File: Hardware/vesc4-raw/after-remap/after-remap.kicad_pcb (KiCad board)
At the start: 4 copper layers, 41.2 x 65 mm, 127 parts, among them K1 SERVO, P1 HALL/Encoder, P101 CANBUS, P2 SWD, P3 PWR_COMM, P4 IN+, P5 IN-, P6 MOTOR1, P7 MOTOR2, P9 MOTOR3, Q1 IPT007N06NATMA1, Q2 IPT007N06NATMA1, Q3 IPT007N06NATMA1, Q4 IPT007N06NATMA1, Q5 IPT007N06NATMA1, Q6 IPT007N06NATMA1, U1 STM32F40X_LQFP64, U2 TC2117, U3 DRV8302, U401 SN65HVD232, X2 8MHz 10ppm

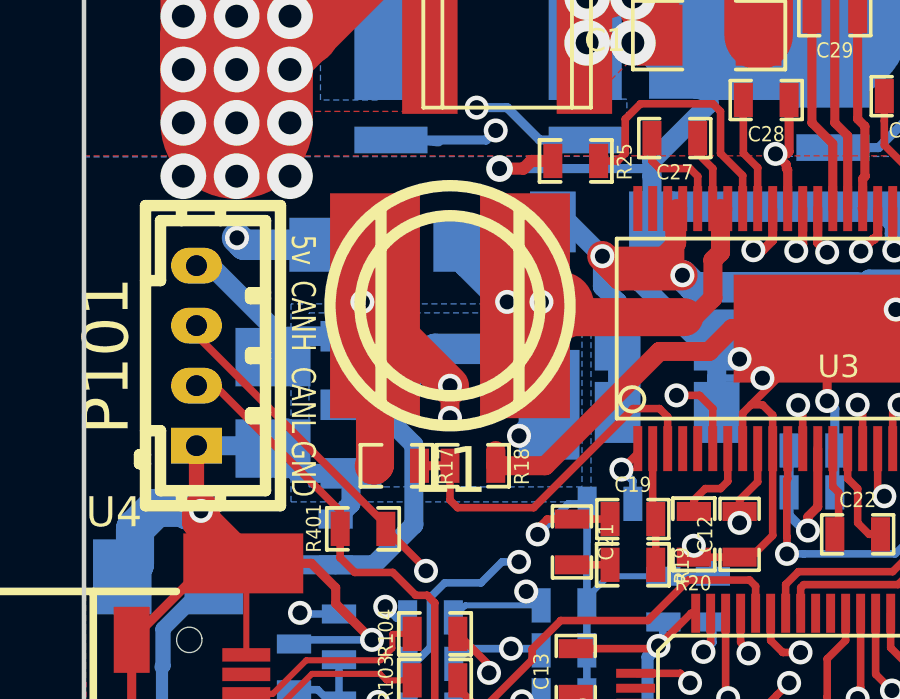
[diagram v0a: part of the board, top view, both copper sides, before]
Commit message: changed inductor
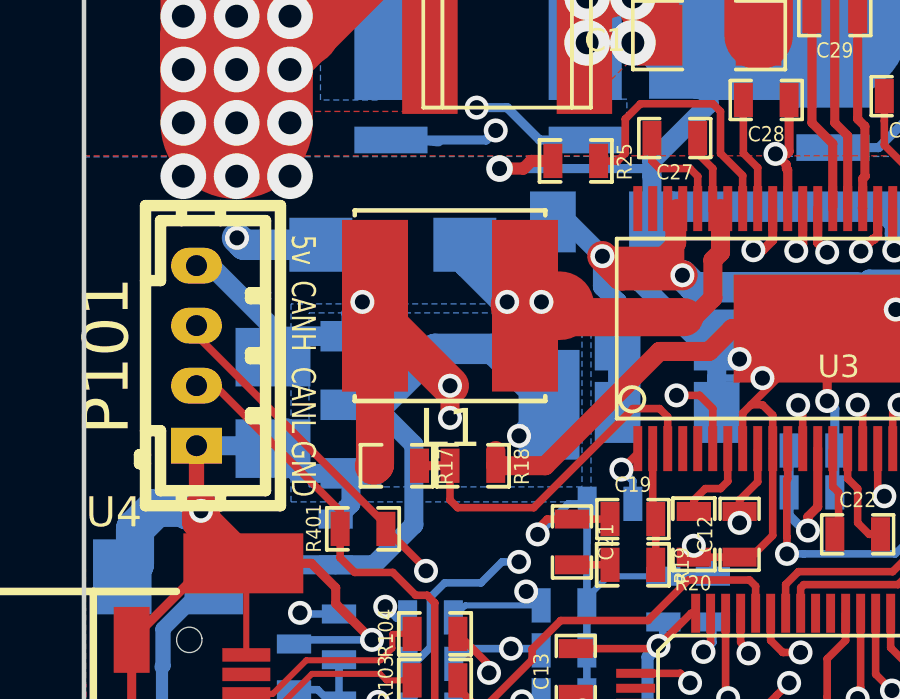
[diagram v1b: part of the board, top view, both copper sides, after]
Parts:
- L1: footprint w_smd_inductors:inductor_smd_8x5mm -> Library:IND-SMD_L6.0-W6.0-shield
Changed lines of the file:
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@@
 		)
 	)
-	(footprint "w_smd_inductors:inductor_smd_8x5mm"
+	(footprint "Library:IND-SMD_L6.0-W6.0-shield"
 		(layer "F.Cu")
 		(at 88.9 115.062 180)
-		(descr "Inductor SMD, d.8mm x h.5mm")
 		(property "Reference" "L1"
-			(at 0 -5.4991 180)
-			(layer "F.SilkS")
-			(effects
-				(font
-					(size 1.524 1.524)
-					(thickness 0.3048)
+			(at 0 -4.0874 180)
+			(layer "F.SilkS")
+			(effects
+				(font
+					(size 1.27 1.27)
+					(thickness 0.15)
 				)
 			)
 		)
 		(property "Value" "22u"
-			(at 0 5.4991 180)
-			(layer "F.SilkS")
-			(hide yes)
-			(effects
-				(font
-					(size 1.524 1.524)
-					(thickness 0.3048)
+			(at 0 4.0874 180)
+			(layer "F.Fab")
+			(effects
+				(font
+					(size 1.27 1.27)
+					(thickness 0.15)
 				)
 			)
@@
 		(sheetfile "Power.kicad_sch")
 		(fp_line
-			(start 2.30124 3.2004)
-			(end 2.30124 -3.2004)
-			(stroke
-				(width 0.381)
-				(type solid)
-			)
-			(layer "F.SilkS")
-		)
-		(fp_line
-			(start -2.30124 -3.2004)
-			(end -2.30124 3.2004)
-			(stroke
-				(width 0.381)
-				(type solid)
+			(start 3.1761 3.1762)
+			(end 3.1761 3.0124)
+			(stroke
+				(width 0.1524)
+				(type default)
+			)
+			(layer "F.SilkS")
+		)
+		(fp_line
+			(start 3.1761 -3.1762)
+			(end 3.1761 -3.0124)
+			(stroke
+				(width 0.1524)
+				(type default)
+			)
+			(layer "F.SilkS")
+		)
+		(fp_line
+			(start -3.1763 3.1762)
+			(end 3.1761 3.1762)
+			(stroke
+				(width 0.1524)
+				(type default)
+			)
+			(layer "F.SilkS")
+		)
+		(fp_line
+			(start -3.1763 3.0124)
+			(end -3.1763 3.1762)
+			(stroke
+				(width 0.1524)
+				(type default)
+			)
+			(layer "F.SilkS")
+		)
+		(fp_line
+			(start -3.1763 -3.0124)
+			(end -3.1763 -3.1762)
+			(stroke
+				(width 0.1524)
+				(type default)
+			)
+			(layer "F.SilkS")
+		)
+		(fp_line
+			(start -3.1763 -3.1762)
+			(end 3.1761 -3.1762)
+			(stroke
+				(width 0.1524)
+				(type default)
 			)
 			(layer "F.SilkS")
 		)
 		(fp_circle
-			(center 0 0)
-			(end -2.99974 0)
-			(stroke
-				(width 0.381)
-				(type solid)
+			(center -2.9999 3)
+			(end -2.9699 3)
+			(stroke
+				(width 0.06)
+				(type default)
 			)
 			(fill no)
-			(layer "F.SilkS")
-		)
-		(fp_circle
-			(center 0 0)
-			(end -4.0005 0)
-			(stroke
-				(width 0.381)
-				(type solid)
-			)
-			(fill no)
-			(layer "F.SilkS")
+			(layer "User.5")
 		)
 		(pad "1" smd rect
-			(at -2.49936 0 180)
-			(size 2.9972 7.49808)
+			(at -2.5 0 180)
+			(size 2.2 5.72)
 			(layers "F.Cu" "F.Mask" "F.Paste")
 			(net 63 "Net-(D4-K)")
 			(pinfunction "1")
 			(pintype "passive")
-			(thermal_bridge_angle 45)
+			(solder_mask_margin 0.0508)
+			(solder_paste_margin 0)
+			(thermal_bridge_angle 0)
 		)
 		(pad "2" smd rect
-			(at 2.49936 0 180)
-			(size 2.9972 7.49808)
+			(at 2.5 0 180)
+			(size 2.2 5.72)
 			(layers "F.Cu" "F.Mask" "F.Paste")
 			(net 1 "+5V")
 			(pinfunction "2")
 			(pintype "passive")
-			(thermal_bridge_angle 45)
+			(solder_mask_margin 0.0508)
+			(solder_paste_margin 0)
+			(thermal_bridge_angle 0)
+		)
+		(zone
+			(net 0)
+			(net_name "")
+			(layer "User.3")
+			(hatch edge 0.5)
+			(priority 100)
+			(connect_pads yes
+				(clearance 0)
+			)
+			(min_thickness 0)
+			(filled_areas_thickness no)
+			(fill yes
+				(thermal_gap 0.5)
+				(thermal_bridge_width 0.5)
+			)
+			(polygon
+				(pts
+					(xy 91.9 112.062) (xy 91.9 118.062) (xy 85.9 118.062) (xy 85.9 112.062)
+				)
+			)
+		)
+		(zone
+			(net 0)
+			(net_name "")
+			(layer "User.4")
+			(hatch edge 0.5)
+			(priority 100)
+			(connect_pads yes
+				(clearance 0)
+			)
+			(min_thickness 0)
+			(filled_areas_thickness no)
+			(fill yes
+				(thermal_gap 0.5)
+				(thermal_bridge_width 0.5)
+			)
+			(polygon
+				(pts
+					(xy 87.45 117.512) (xy 85.9 117.512) (xy 85.9 112.612) (xy 87.45 112.612)
+				)
+			)
+		)
+		(zone
+			(net 0)
+			(net_name "")
+			(layer "User.4")
+			(hatch edge 0.5)
+			(priority 100)
+			(connect_pads yes
+				(clearance 0)
+			)
+			(min_thickness 0)
+			(filled_areas_thickness no)
+			(fill yes
+				(thermal_gap 0.5)
+				(thermal_bridge_width 0.5)
+			)
+			(polygon
+				(pts
+					(xy 90.35 112.612) (xy 91.9 112.612) (xy 91.9 117.512) (xy 90.35 117.512)
+				)
+			)
 		)
 		(embedded_fonts no)
-		(model "walter/smd_inductors/inductor_smd_8x5mm.wrl"
+		(model "${KIPRJMOD}/EASYEDA_MODELS/IND-SMD_L6.0-W6.0-H4.5.step"
 			(offset
-				(xyz 0 0 0)
+				(xyz 0.0001 -0 0)
 			)
 			(scale
@@
 			)
 			(rotate
-				(xyz 0 0 0)
-			)
-		)
+				(xyz -0 -0 -90)
+			)
+		)

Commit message: checkpoint dapetin komponen kristal
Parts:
- added ?: C521686, Library:C521686, B.Cu at (98.6, 143.3)

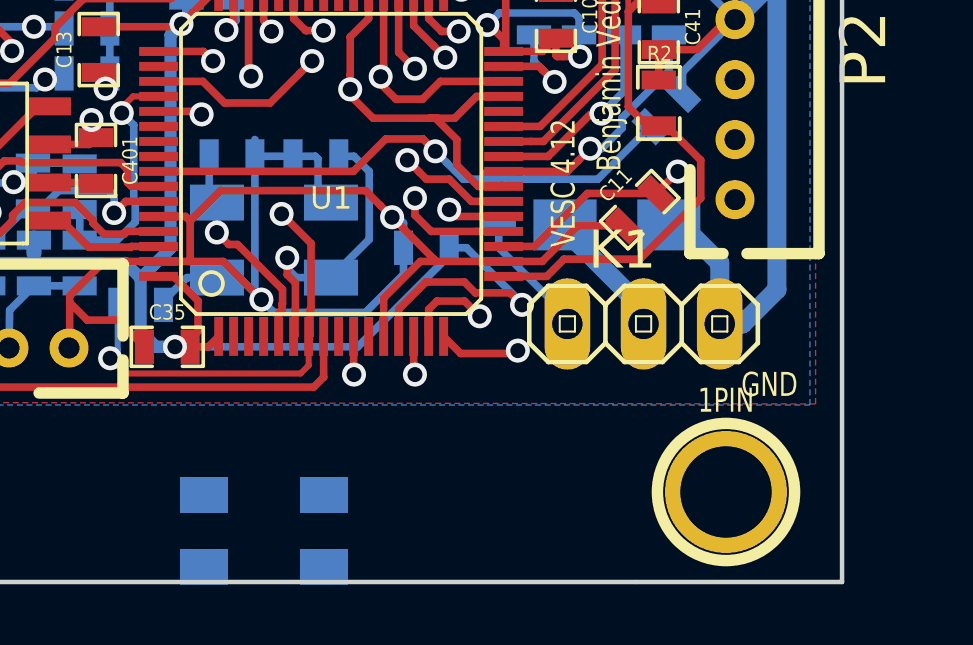
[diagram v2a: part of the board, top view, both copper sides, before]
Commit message: changed crystal x2
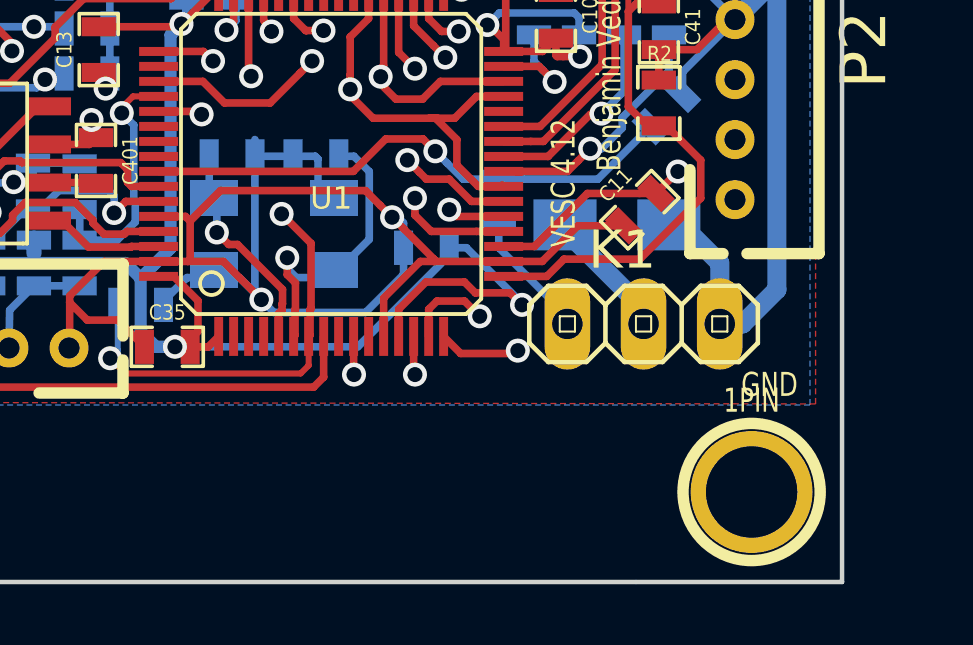
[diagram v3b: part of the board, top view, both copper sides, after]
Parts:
- removed ?: C521686, Library:C521686
- X2: value 8MHz 10ppm -> 5TJ480000NYLBC; footprint CRF1:Crystal_5x3mm -> Library:C2149245
- moved 1PIN 0.85 mm to (114.9, 142.0)
- moved X2 0.20 mm to (98.9, 133.4)
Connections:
- net Net-(U1-PH0-OSC_IN) renamed /MCU/X2-1
- C38 pad 1: Net-(U1-PH1-OSC_OUT) -> /MCU/X2-2
- U1 pad 6: Net-(U1-PH1-OSC_OUT) -> /MCU/X2-2
- X2 pad 2: Net-(U1-PH1-OSC_OUT) -> GND
- X2 pad 3: GND -> /MCU/X2-2
- X2 pad 4: (no net) -> GND
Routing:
- net Net-(U1-PH1-OSC_OUT): track 9.99 -> 0.00 mm, vias 1 -> 0
- net /MCU/X2-2: track 0.00 -> 9.99 mm, vias 0 -> 1
- net GND: track 396.9 -> 397.8 mm

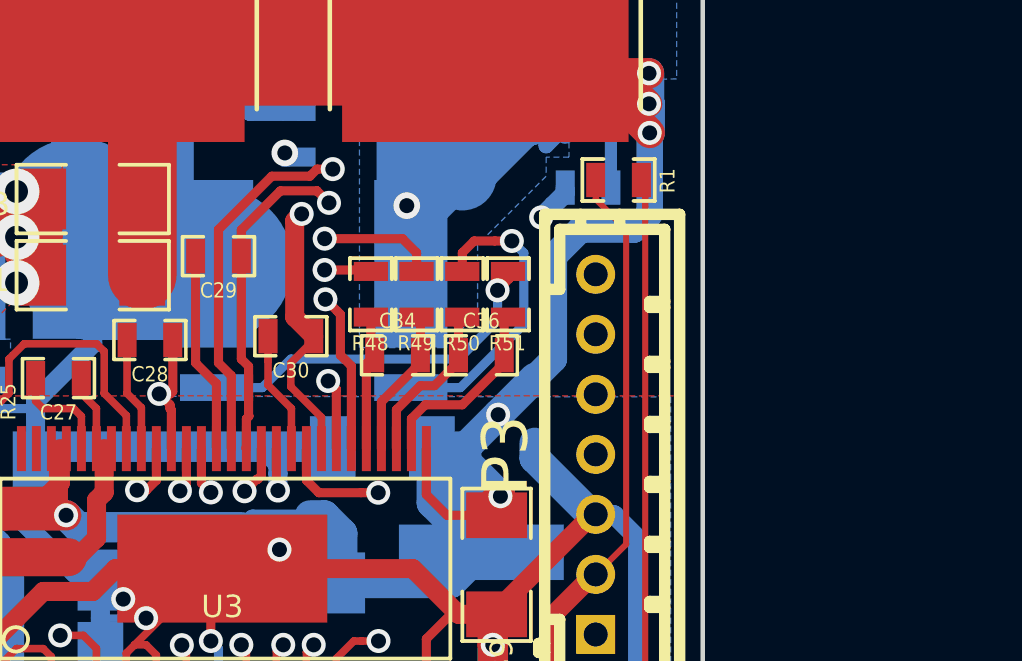
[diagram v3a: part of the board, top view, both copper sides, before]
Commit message: checkpoint ganti shunt
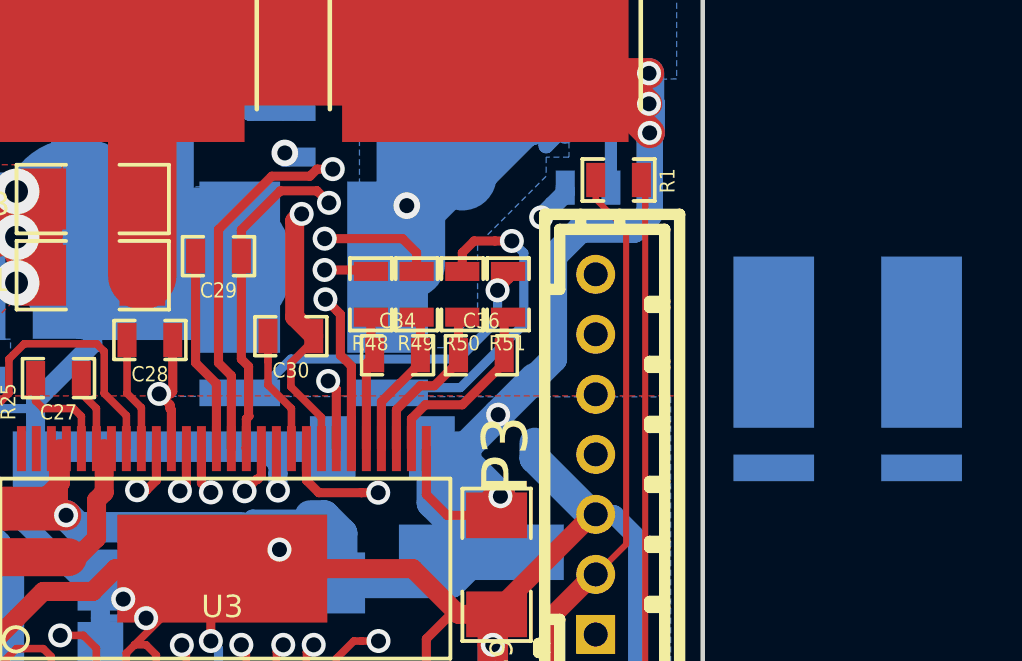
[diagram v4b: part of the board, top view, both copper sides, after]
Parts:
- added R54: WSLP27262L000FEA, Library:C2076510, B.Cu at (122.7, 110.4)
- R53: value SHUNT -> WSLP27262L000FEA; footprint CRF1:WSLP2726 -> Library:C2076510
- moved R53 0.84 mm to (104.9, 107.9)
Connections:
- R53 pad 1: GND -> /Mosfet driver/SH2_B
- R53 pad 2: /Power MOSFETS/Q2-s -> /Mosfet driver/SH2_A
- R53 pad 3: /Mosfet driver/SH2_B -> GND
- R53 pad 4: /Mosfet driver/SH2_A -> /Power MOSFETS/Q2-s

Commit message: ganti shunt
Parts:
- removed the R54 at (90.2, 108.5)
- moved R54 32.2 mm to (90.6, 107.4)
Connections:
- R54 pad 1: /Mosfet driver/SH1_B -> /Mosfet driver/SH1_A
- R54 pad 2: /Mosfet driver/SH1_A -> /Mosfet driver/SH1_B
- R54 pad 3: unconnected-(R54-Pad3) -> /Power MOSFETS/Q6-s
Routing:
- net /Mosfet driver/M_L3: track 20.0 -> 21.1 mm

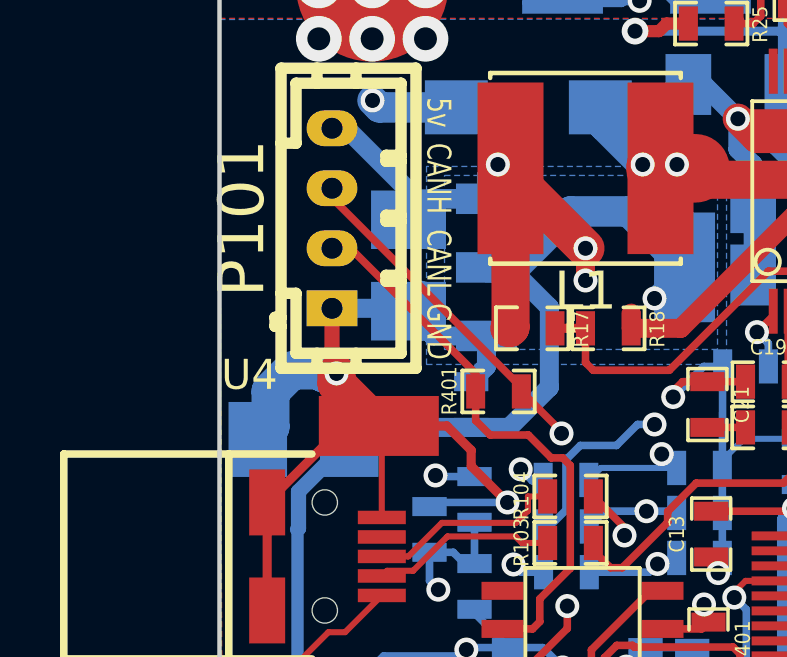
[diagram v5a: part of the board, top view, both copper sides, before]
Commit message: changed c tantalum
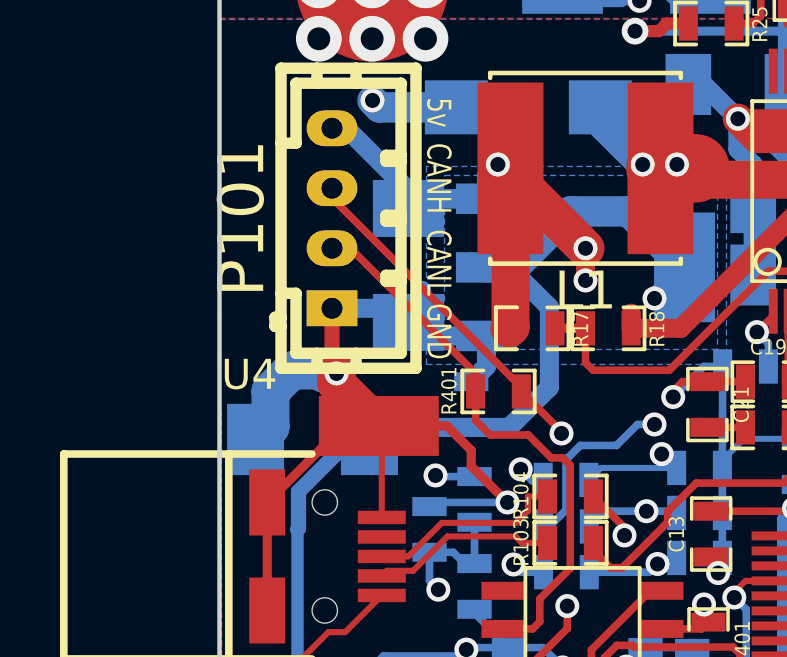
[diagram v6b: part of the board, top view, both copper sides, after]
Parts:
- C25, C33: footprint w_smd_cap:c_tant_B -> Library:CAP-SMD_L3.5-W2.8-R-RD
- moved C25 0.30 mm to (79.8, 124.1)

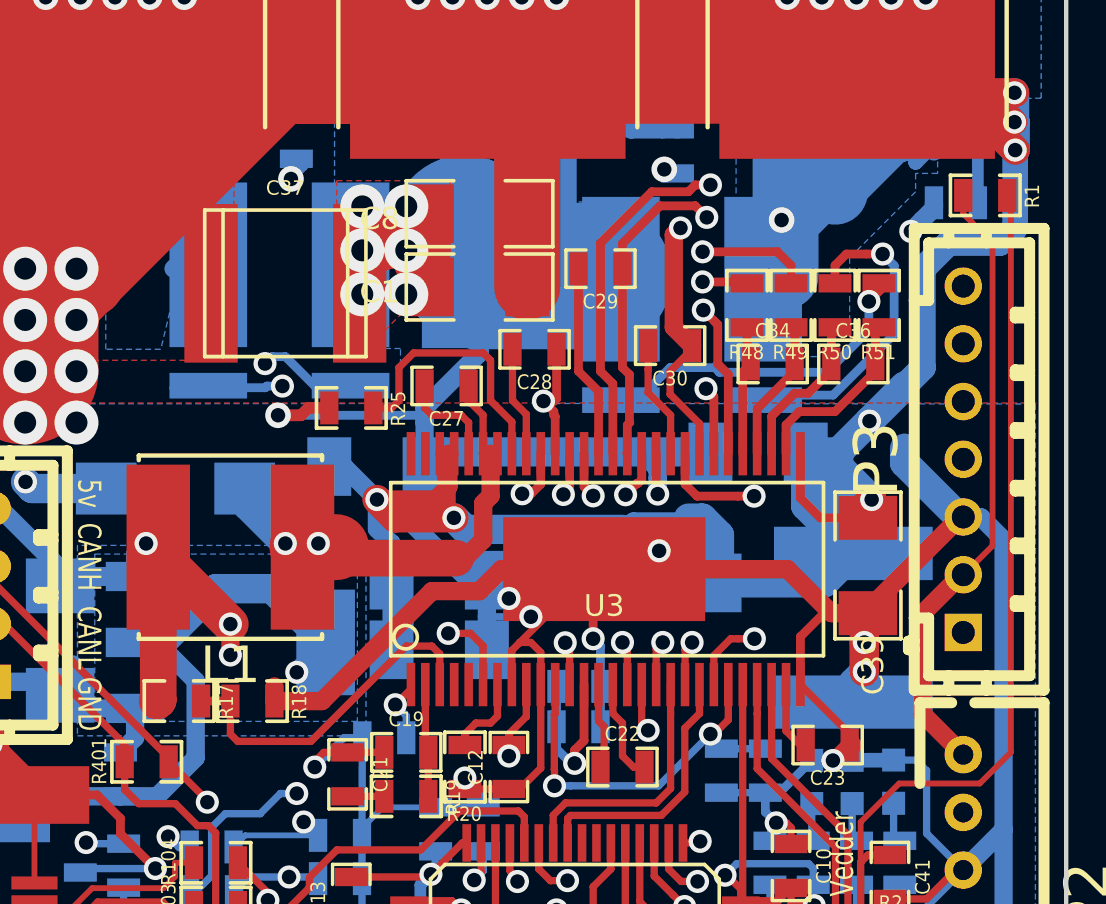
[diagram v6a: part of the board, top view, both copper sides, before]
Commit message: changed 15u 100V footprint
c37 c51
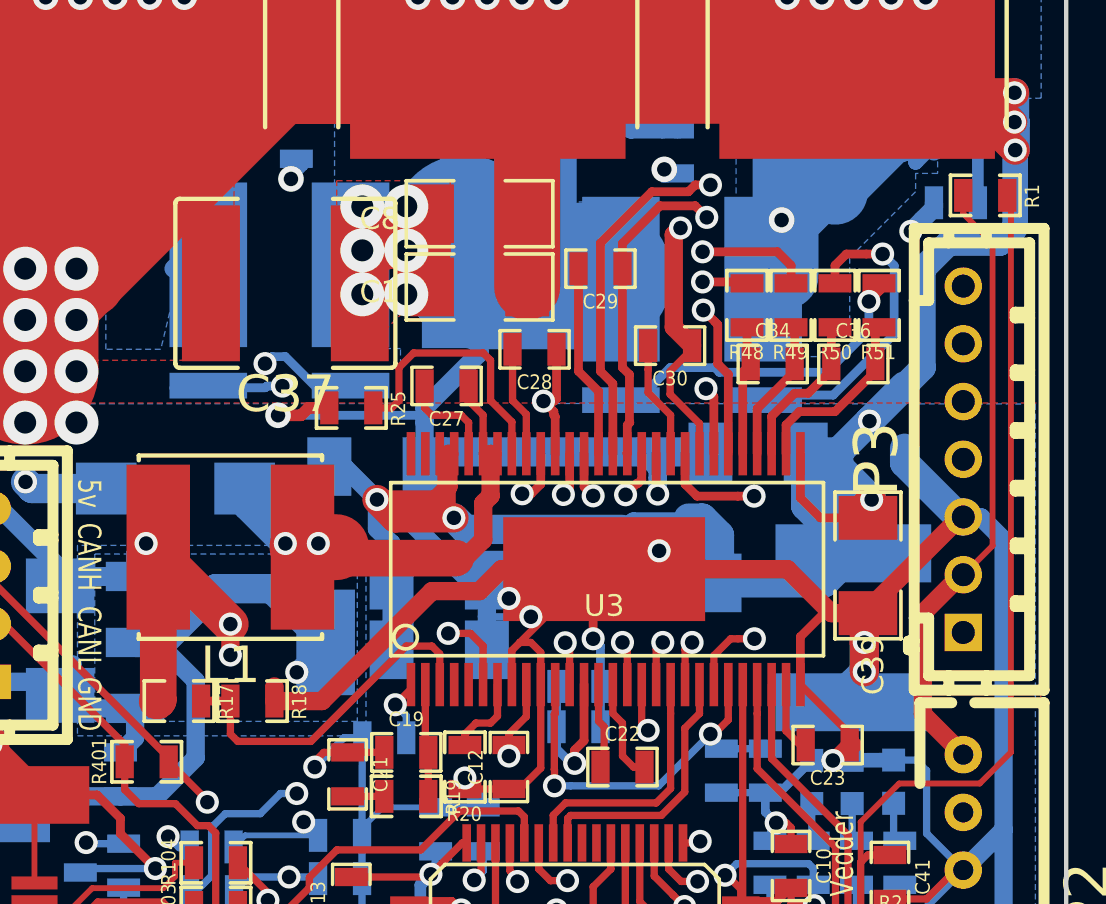
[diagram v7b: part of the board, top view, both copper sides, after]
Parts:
- C37, C51: footprint w_smd_cap:c_2220 -> Library:C2220_L5.6-W5.0-H3.0
- turned C37 to 180 degrees
- turned C51 to 90 degrees
